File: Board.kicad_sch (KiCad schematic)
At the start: 10 parts, among them J1 WAGO 2086-1202, J2 WAGO 2086-1202, J3 WAGO 2086-1230, J4 WAGO 2086-1230, SW1 500SSP1S1M6QEA

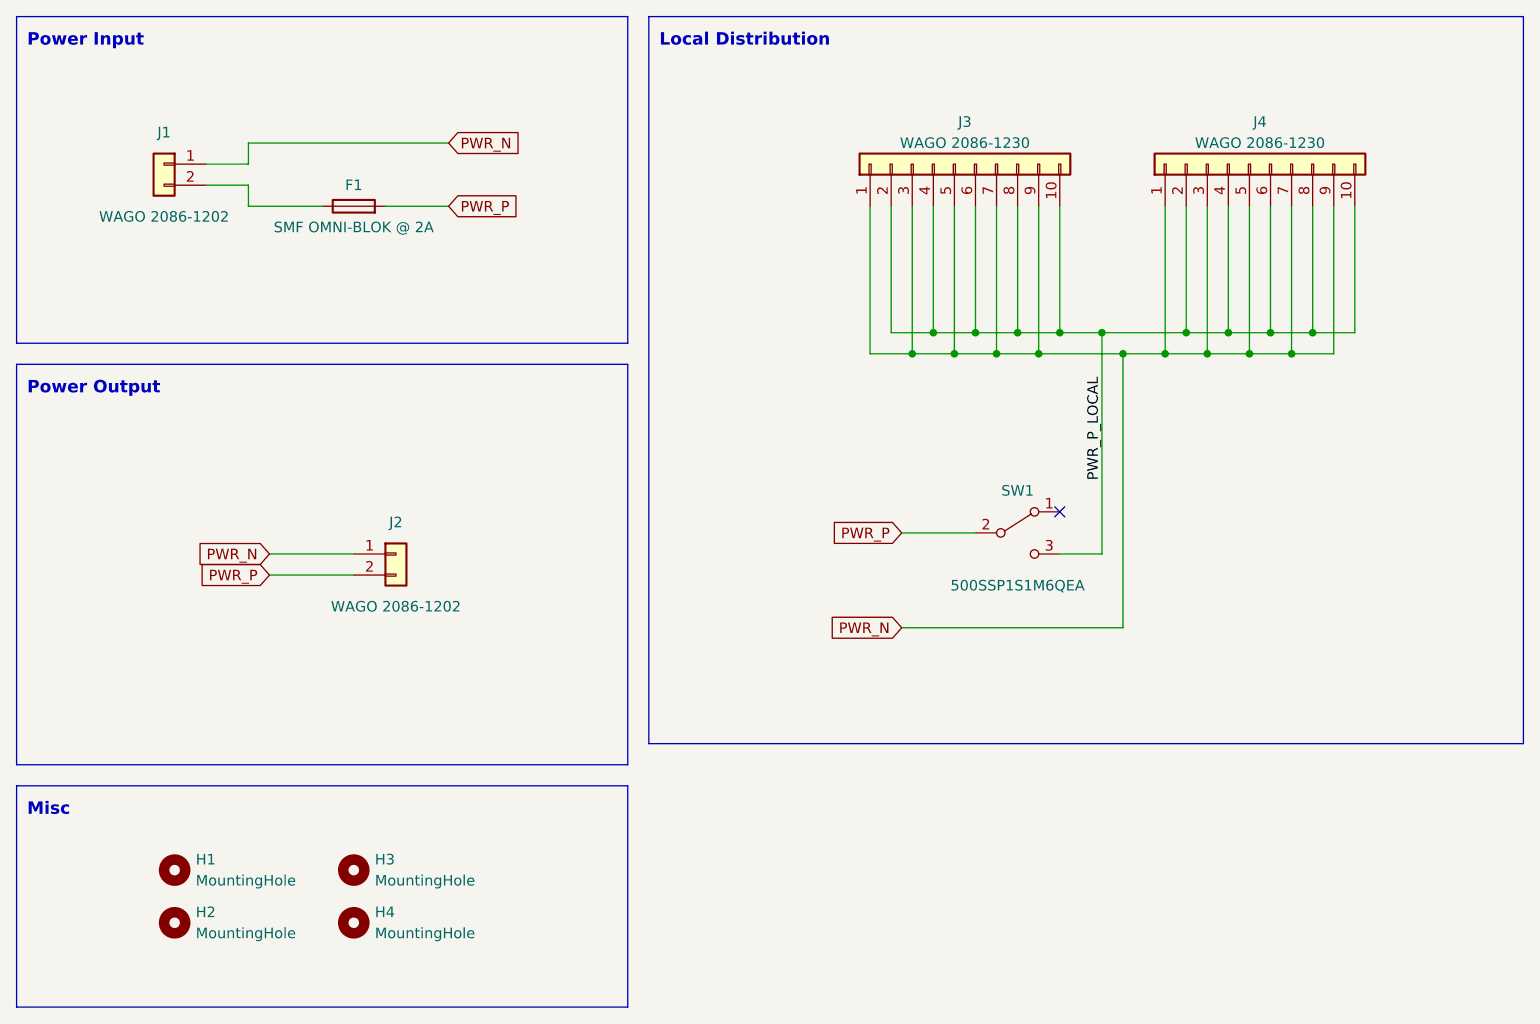
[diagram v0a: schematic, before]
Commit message: update to KiCad 7
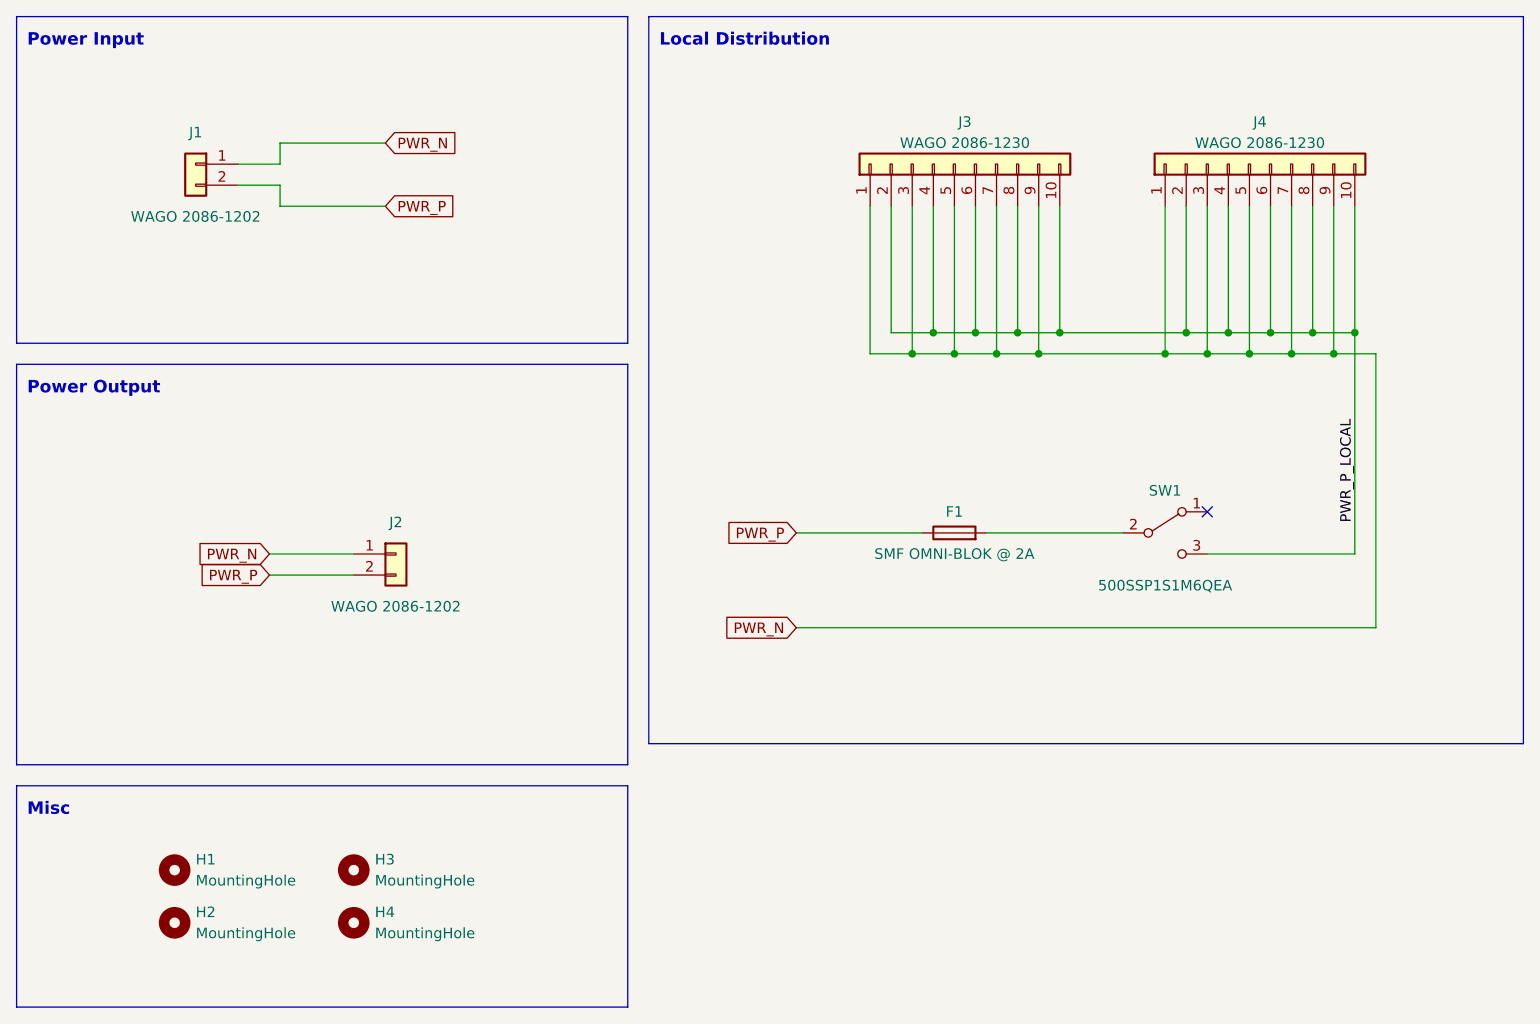
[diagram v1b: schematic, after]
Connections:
- net PWR_P: now also F1.1, J1.2 (Pin_2); no longer F1.2, SW1.2 (B)
- new net: F1.2, SW1.2 (B)
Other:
- moved on the sheet: F1, J1, SW1
